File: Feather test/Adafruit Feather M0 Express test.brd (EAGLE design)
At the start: 89 x 22.9 mm, 45 parts, among them SW1 SPST_TACT-KMR2, U1 2MB Flash, U2 AP2112-3.3, U3 NAU7802, U4 LMV324, X1 20317, X2 32.768, X3 microUSB

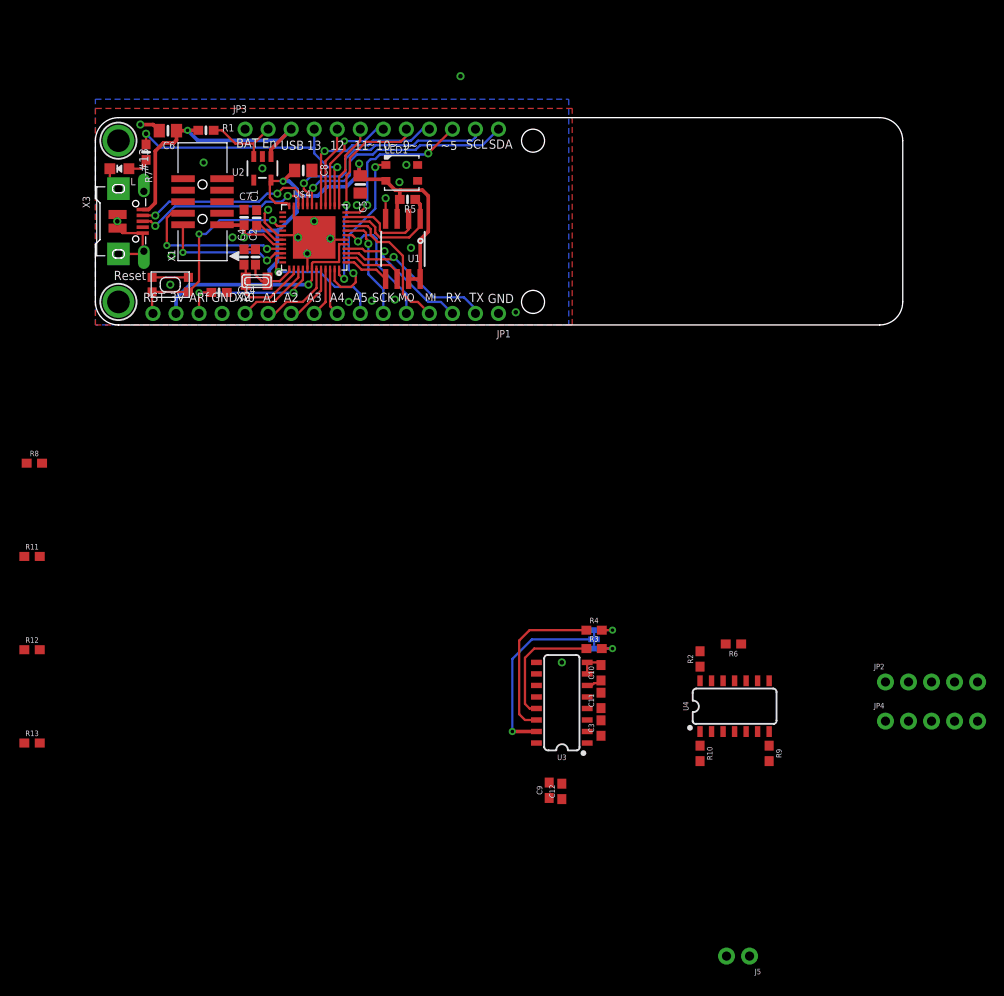
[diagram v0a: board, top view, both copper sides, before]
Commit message: Wheatstone ordered
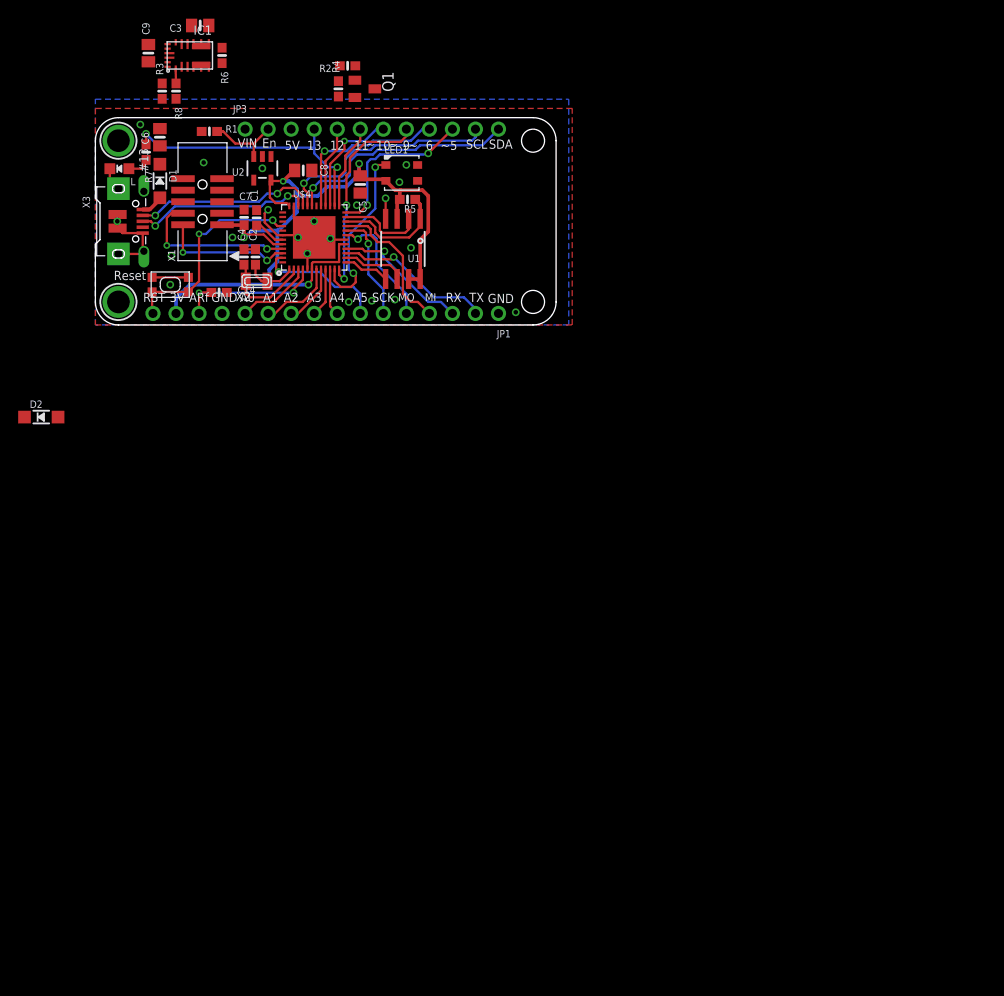
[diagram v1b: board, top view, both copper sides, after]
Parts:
- removed C10, C11: 0.1uF, SparkFun-Capacitors:0603
- removed C12: 1.0uF, SparkFun-Capacitors:0603
- removed J5: (no value), SparkFun-Connectors:1X02_NO_SILK
- removed JP2, JP4: (no value), SparkFun-Connectors:1X05_NO_SILK
- removed JP5: I2C, SparkFun-Jumpers:SMT-JUMPER_3_2-NC_TRACE_SILK
- removed R10, R9: 47, SparkFun-Resistors:0603
- removed R11, R12, R13: 100, SparkFun-Resistors:0603
- removed U3: NAU7802, SparkFun-IC-Conversion:SO16
- removed U4: LMV324, SparkFun-IC-Amplifiers:SO14
- added D1, D2: MBR120, microbuilder:SOD-123
- added IC1: MPM3610, microbuilder:MPM3610
- added Q1: BSS138, adafruit:SOT23
- C3, C9: value 0.1uF -> 22uF; device SparkFun-Capacitors:0603 -> microbuilder:0805-NO
- R2: value 47 -> 10K; device SparkFun-Resistors:0603 -> microbuilder:0603-NO
- R3: value 2.2k -> 100K; device SparkFun-Resistors:0603 -> microbuilder:0603-NO
- R4: value 2.2k -> 10K; device SparkFun-Resistors:0603 -> microbuilder:0603-NO
- R6: value 47 -> 100K; device SparkFun-Resistors:0603 -> microbuilder:0603-NO
- R8: value 100 -> 18.7K; device SparkFun-Resistors:0603 -> microbuilder:0603-NO
- moved C9 92.5 mm to (5.84, 30.0)
- moved C3 89.2 mm to (11.6, 33.0), turned to 180 degrees
- moved R6 86.0 mm to (14.0, 29.7), turned to 270 degrees
- moved R3 77.8 mm to (7.37, 25.8), turned to 90 degrees
- moved R2 76.1 mm to (27.8, 28.6), turned to 180 degrees
- moved R4 66.0 mm to (26.8, 26.0), turned to 90 degrees
- moved R8 43.9 mm to (8.89, 25.8), turned to 270 degrees
- moved C6 1.14 mm to (7.11, 20.7), turned to 90 degrees
- moved R1 0.40 mm to (12.6, 21.3)
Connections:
- removed net 3.3V: JP5.2, U3.15
- removed net A+: JP4.2, U4.3
- removed net A-: JP4.3, U4.5
- removed net B+: JP2.2, U4.10
- removed net B-: JP2.3, U4.12
- removed net GAIN_A-: R8.1, U4.6
- removed net GAIN_B+: R13.1, U4.9
- removed net GAIN_B-: R12.1, U4.13
- removed net INT: J5.2, U3.12
- removed net N$10: R8.2, R9.1, U4.7
- removed net N$11: C10.1, U3.6
- removed net N$12: C3.2, R10.2, U3.3
- removed net N$13: C3.1, R9.2, U3.2
- removed net N$14: C11.2, R6.2, U3.5
- removed net N$15: C11.1, R2.2, U3.4
- removed net N$3: JP5.1, R4.2
- removed net N$4: JP5.3, R3.2
- removed net N$6: R12.2, R2.1, U4.14
- removed net N$8: R11.1, U4.2
- removed net N$9: R10.1, R11.2, U4.1
- removed net VBAT: JP3.1
- removed net VDDA: C12.1, C9.1, J5.1, JP2.5, JP4.5, U3.1, U3.16
- new net +5V: C3.1, D2.A, IC1.7, IC1.8, IC1.9, JP3.3, R2.2, R6.1
- new net D12_5V: Q1.3, R2.1
- new net FB: IC1.1, R6.2, R8.1
- new net SW: IC1.4, IC1.5, IC1.6
- new net VCC: IC1.2
- new net VIN: C9.1, IC1.16, JP3.1, R3.1
- net +3V3: now also Q1.1, R4.2
- net D12: now also Q1.2, R4.1
- net EN: now also IC1.17, R3.2
- net GND: now also C3.2, IC1.12, IC1.13, IC1.14, IC1.3, R8.2; no longer C10.2, C12.2, JP2.1, JP2.4, JP4.1, JP4.4, U3.7, U3.8, U3.9
- net N$1: now also C6.1, D1.C, D2.C, R1.1, U2.1; no longer R13.2, R6.1, U4.8
- net SCL: no longer R3.1, U3.13
- net SDA: no longer R4.1, U3.14
- net VBUS: now also D1.A; no longer C6.1, JP3.3, R1.1, U2.1
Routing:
- net VBUS: track 30.1 -> 3.23 mm, vias 1 -> 0
- net 3.3V: track 20.6 -> 0.00 mm, vias 1 -> 0
- net SDA: track 44.2 -> 26.1 mm
- net SCL: track 39.2 -> 25.5 mm
- net GND: track 44.9 -> 39.6 mm, vias 23 -> 21
- net N$3: track 3.22 -> 0.00 mm, vias 1 -> 0
- net N$4: track 3.21 -> 0.00 mm, vias 1 -> 0
- net N$11: track 1.74 -> 0.00 mm
- net FB: track 0.00 -> 1.64 mm
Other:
- board size 89 x 22.9 mm -> 50.8 x 22.9 mm
- board text added: "5V"
- board text added: "VIN"
